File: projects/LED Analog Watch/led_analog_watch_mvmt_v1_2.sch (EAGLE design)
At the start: 47 parts, among them IC1 ATMEGA644M, IC2 FT232RQ, U2 MCP73831, Y1 32kHz

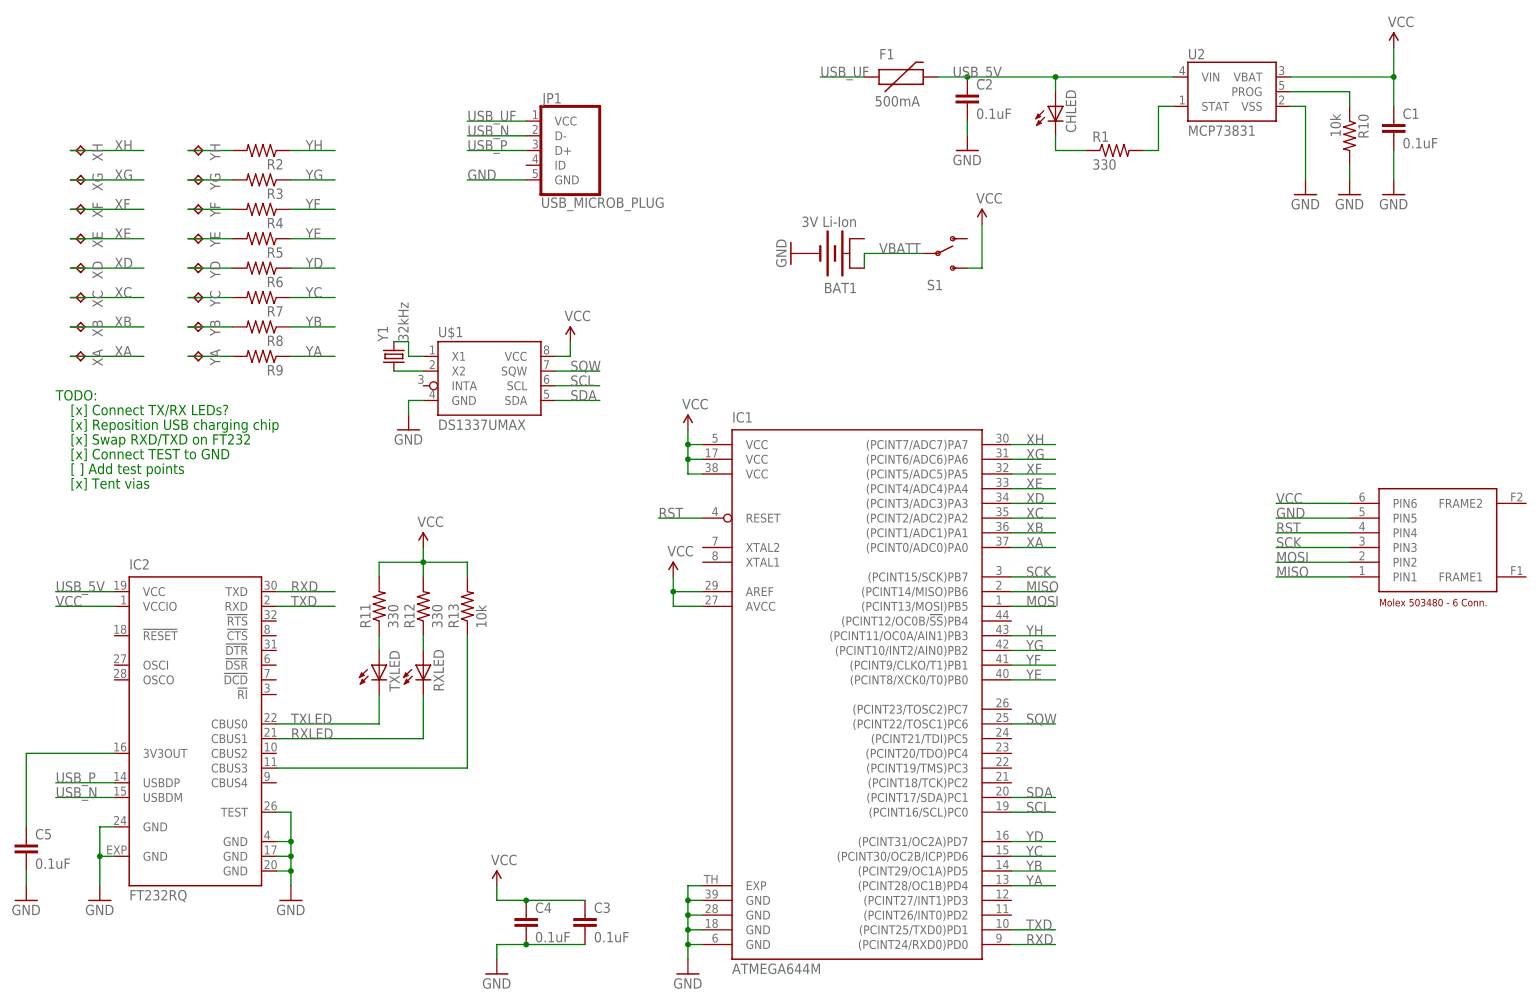
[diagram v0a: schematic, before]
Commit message: Minor adjustments to schematic and docs
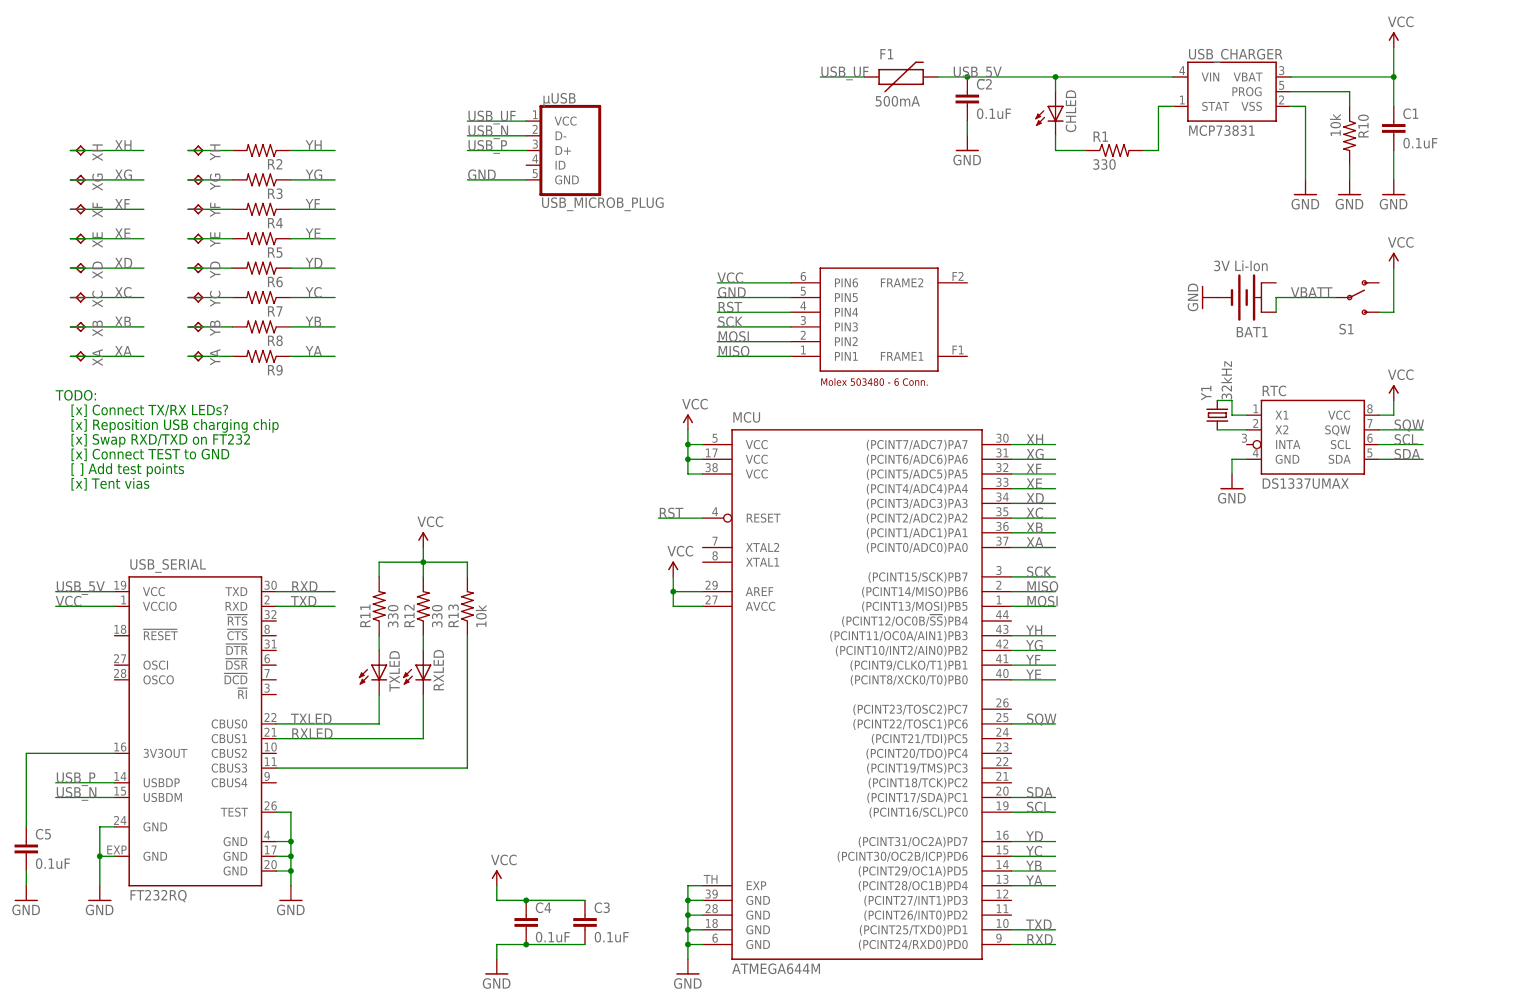
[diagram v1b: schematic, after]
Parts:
- removed U$1: DS1337UMAX, jcole:DS1337UMAX
- added RTC: DS1337UMAX, jcole:DS1337UMAX
- renumbered IC1 to MCU, IC2 to USB_SERIAL, JP1 to µUSB, U2 to USB_CHARGER
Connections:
- net GND: now also RTC.GND; no longer U$1.GND
- net N$14: now also RTC.X2; no longer U$1.X2
- net N$15: now also RTC.X1; no longer U$1.X1
- net SCL: now also RTC.SCL; no longer U$1.SCL
- net SDA: now also RTC.SDA; no longer U$1.SDA
- net SQW: now also RTC.SQW; no longer U$1.SQW
- net VCC: now also RTC.VCC; no longer U$1.VCC
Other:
- moved on the sheet: BAT1, S1, Y1
